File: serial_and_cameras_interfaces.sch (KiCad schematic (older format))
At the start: 60 parts, among them J13 533980471, J15 533980471, J16 533980471, J17 533980471, J2 WE_68715014522, U16 NTS0102GT, U17 NTS0104PW,118, U18 MAX485EESA, U5 NTS0102GT, U6 PCA9547BS

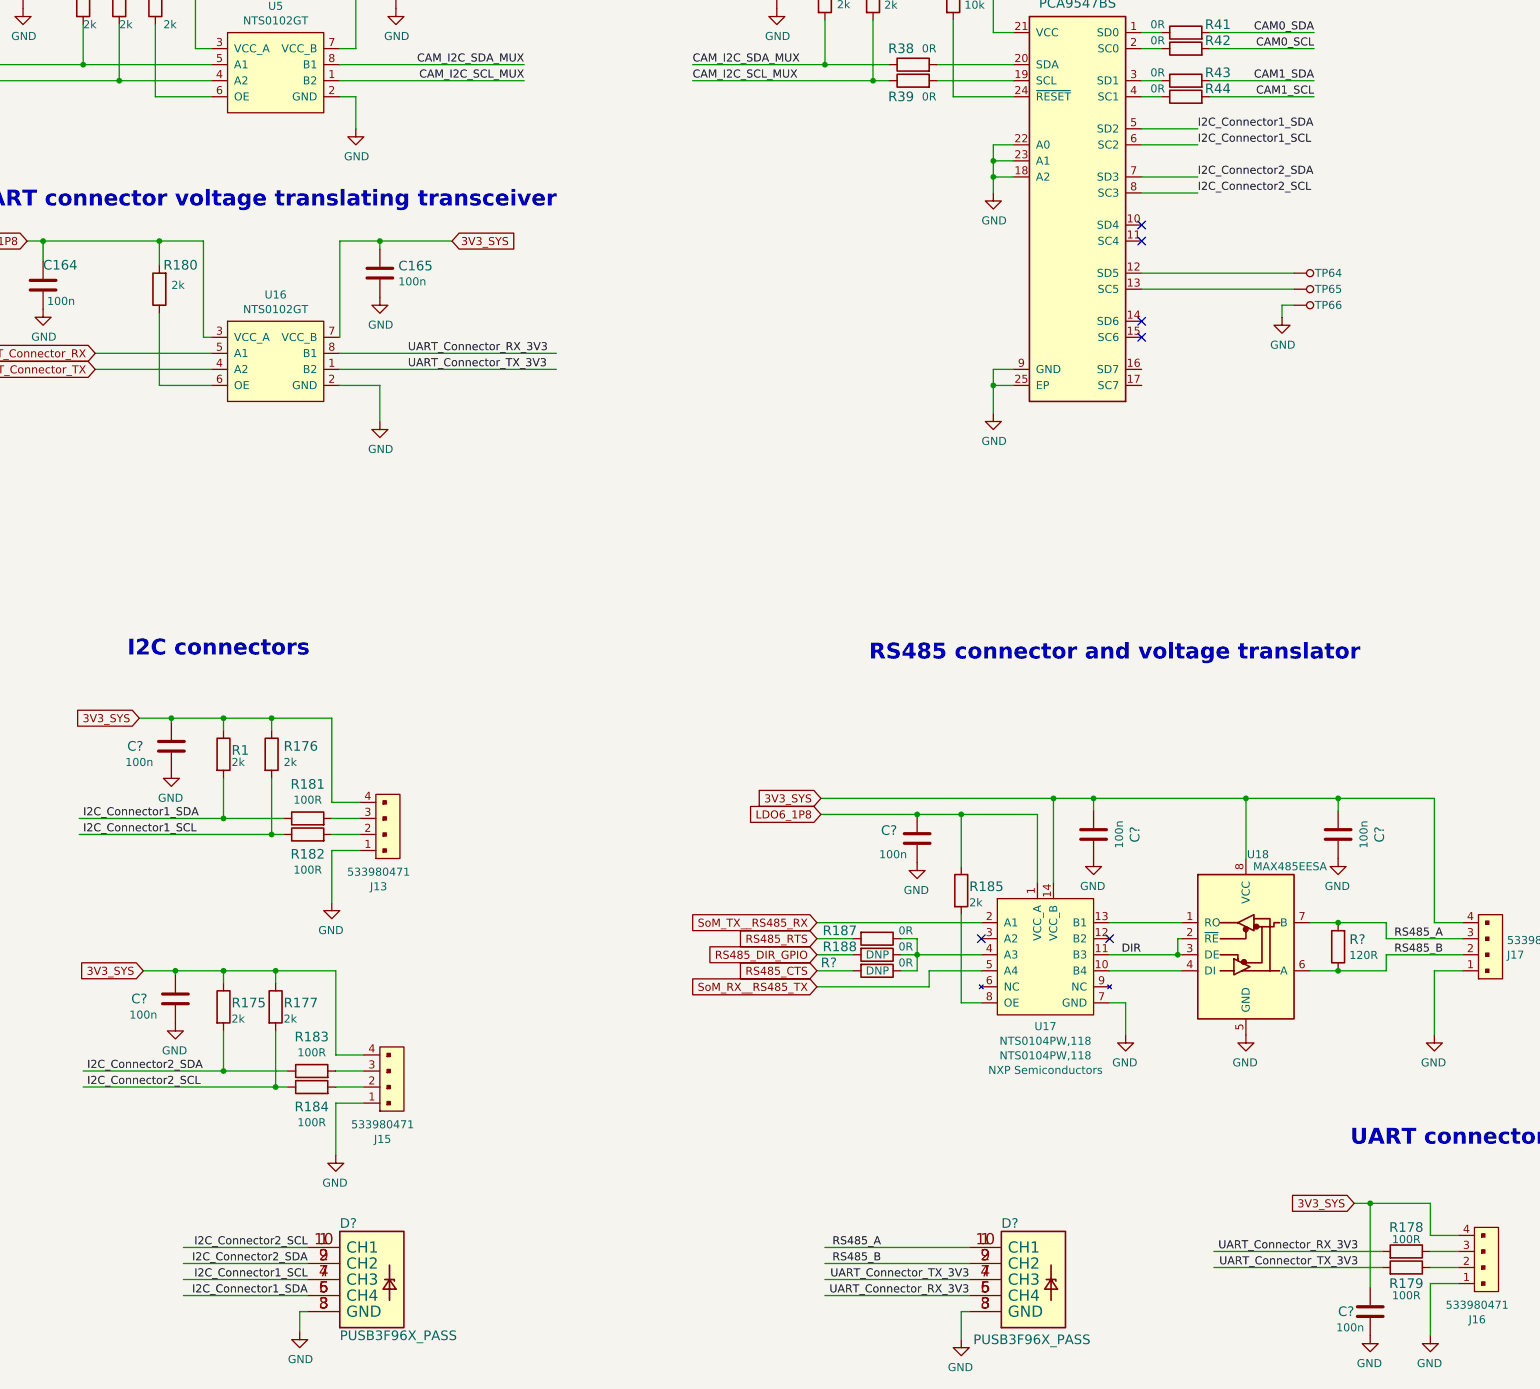
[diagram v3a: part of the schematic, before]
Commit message: Placement of serial interface connectors components
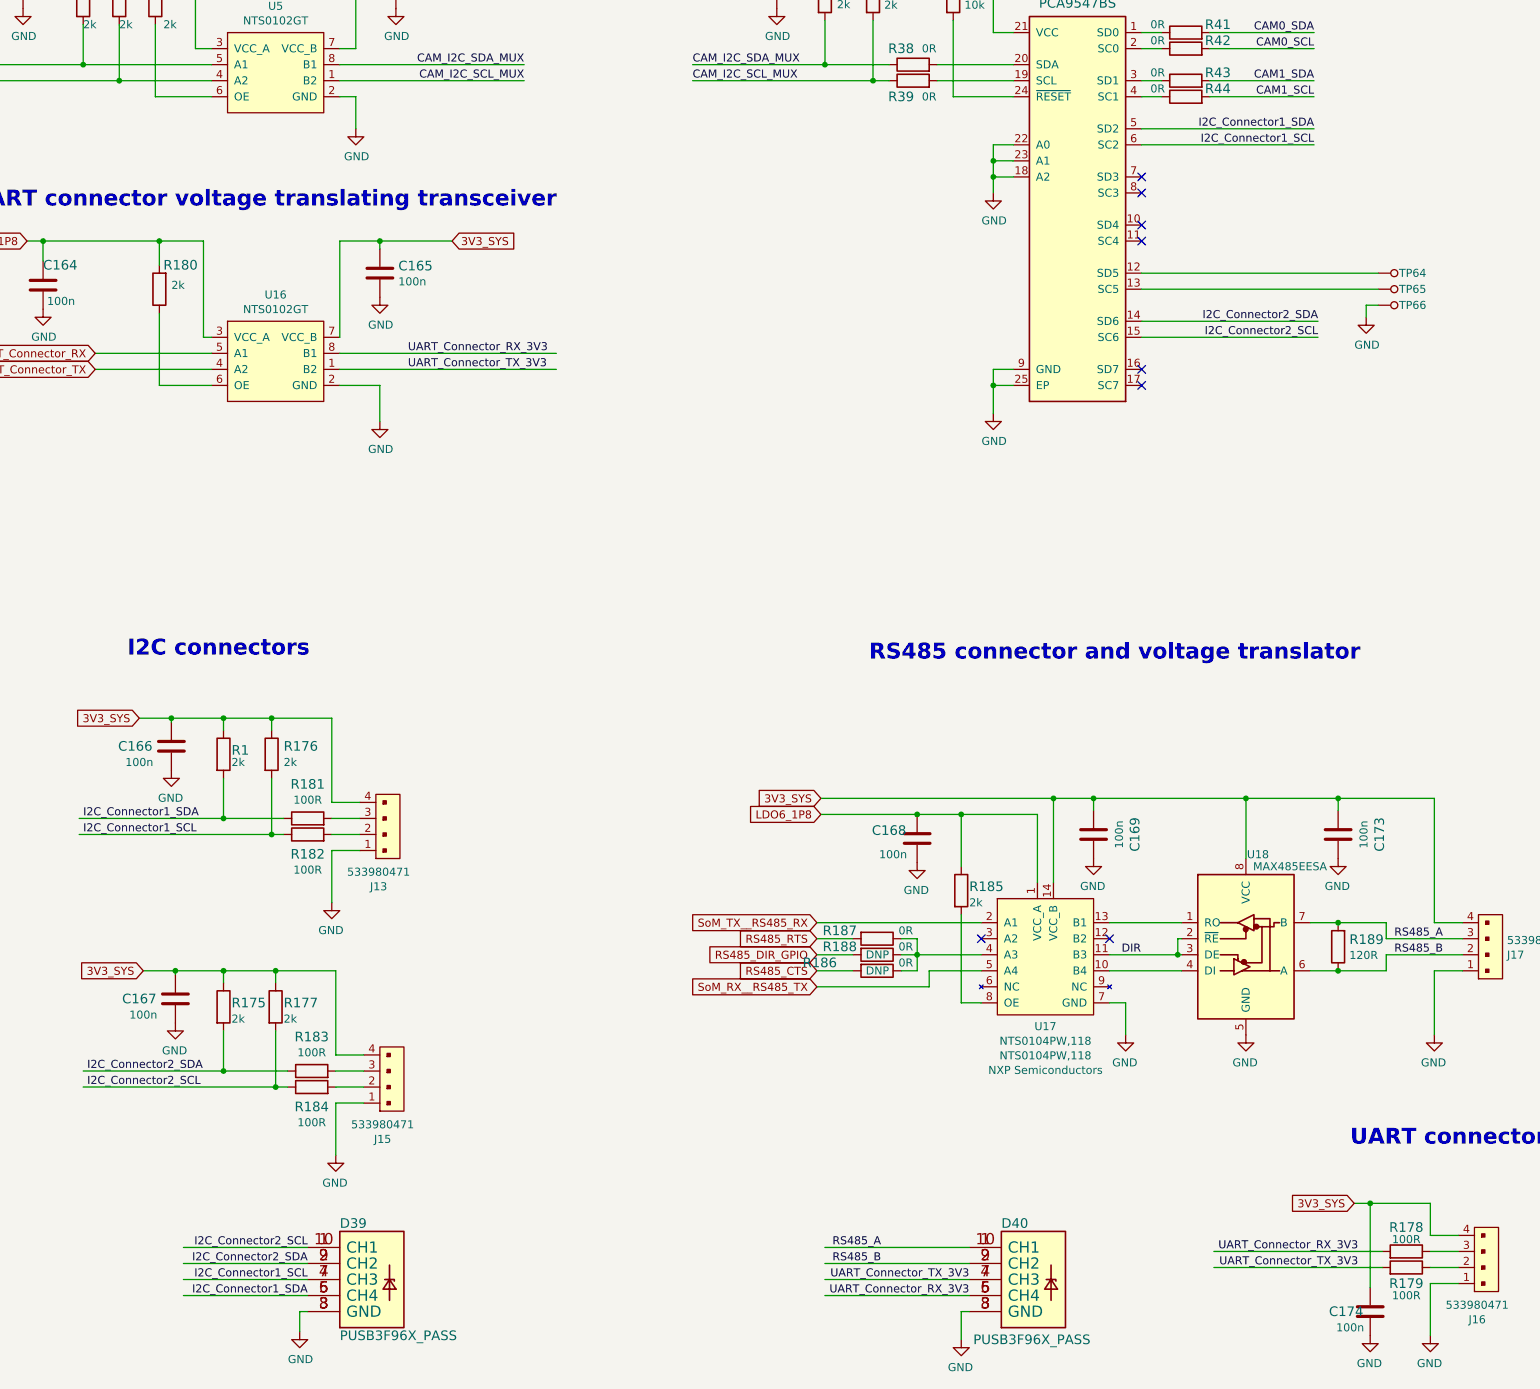
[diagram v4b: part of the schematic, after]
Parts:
- gave numbers to parts that had none: 10
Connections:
- no-connect marks 20 -> 22
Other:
- moved on the sheet: TP64, TP65, TP66
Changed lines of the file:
@@
 NoConn ~ 8750 3325
 NoConn ~ 8750 3425
-NoConn ~ 8750 3925
-NoConn ~ 8750 4025
 $Comp
 L sc606-baseboard:R_0R_0402 R41
@@
 Camera connector\n
 Wire Wire Line
-	8750 2725 9100 2725
-Wire Wire Line
-	8750 2825 9100 2825
+	8750 2725 9825 2725
+Wire Wire Line
+	8750 2825 9825 2825
 $Comp
 L sc606-baseboard:TP_SMD_0_75MM TP?
 U 1 1 640131A9
-P 9800 3625
+P 10325 3625
 AR Path="/61D43102/640131A9" Ref="TP?"  Part="1"
 AR Path="/61D49F95/640131A9" Ref="TP64"  Part="1"
-F 0 "TP64" V 9800 3425 50  0000 L CNN
-F 1 "TP_SMD_1_5MM" H 9800 3525 50  0001 C CNN
-F 2 "sc606-baseboard-footprints:TP-R-1.5" H 10000 3825 60  0001 L CNN
-F 3 "" H 10000 3925 60  0001 L CNN
-	1    9800 3625
+F 0 "TP64" V 10325 3425 50  0000 L CNN
+F 1 "TP_SMD_1_5MM" H 10325 3525 50  0001 C CNN
+F 2 "sc606-baseboard-footprints:TP-R-1.5" H 10525 3825 60  0001 L CNN
+F 3 "" H 10525 3925 60  0001 L CNN
+	1    10325 3625
 	0    -1   -1   0
 $EndComp
@@
 L sc606-baseboard:TP_SMD_0_75MM TP?
 U 1 1 640131AF
-P 9800 3725
+P 10325 3725
 AR Path="/61D43102/640131AF" Ref="TP?"  Part="1"
 AR Path="/61D49F95/640131AF" Ref="TP65"  Part="1"
-F 0 "TP65" V 9800 3525 50  0000 L CNN
-F 1 "TP_SMD_1_5MM" H 9800 3625 50  0001 C CNN
-F 2 "sc606-baseboard-footprints:TP-R-1.5" H 10000 3925 60  0001 L CNN
-F 3 "" H 10000 4025 60  0001 L CNN
-	1    9800 3725
+F 0 "TP65" V 10325 3525 50  0000 L CNN
+F 1 "TP_SMD_1_5MM" H 10325 3625 50  0001 C CNN
+F 2 "sc606-baseboard-footprints:TP-R-1.5" H 10525 3925 60  0001 L CNN
+F 3 "" H 10525 4025 60  0001 L CNN
+	1    10325 3725
 	0    -1   -1   0
 $EndComp
 Wire Wire Line
-	8750 3625 9700 3625
-Wire Wire Line
-	8750 3725 9700 3725
+	8750 3625 10225 3625
+Wire Wire Line
+	8750 3725 10225 3725
 $Comp
 L sc606-baseboard:TP_SMD_0_75MM TP?
 U 1 1 640131B7
-P 9800 3825
+P 10325 3825
 AR Path="/61D43102/640131B7" Ref="TP?"  Part="1"
 AR Path="/61D49F95/640131B7" Ref="TP66"  Part="1"
-F 0 "TP66" V 9800 3625 50  0000 L CNN
-F 1 "TP_SMD_1_5MM" H 9800 3725 50  0001 C CNN
-F 2 "sc606-baseboard-footprints:TP-R-1.5" H 10000 4025 60  0001 L CNN
-F 3 "" H 10000 4125 60  0001 L CNN
-	1    9800 3825
+F 0 "TP66" V 10325 3625 50  0000 L CNN
+F 1 "TP_SMD_1_5MM" H 10325 3725 50  0001 C CNN
+F 2 "sc606-baseboard-footprints:TP-R-1.5" H 10525 4025 60  0001 L CNN
+F 3 "" H 10525 4125 60  0001 L CNN
+	1    10325 3825
 	0    -1   -1   0
 $EndComp
 Wire Wire Line
-	9700 3825 9625 3825
-Wire Wire Line
-	9625 3825 9625 3900
+	10225 3825 10150 3825
+Wire Wire Line
+	10150 3825 10150 3900
 $Comp
 L sc606-baseboard:GND #PWR0228
 U 1 1 640131BF
-P 9625 3900
-F 0 "#PWR0228" H 9625 3650 50  0001 C CNN
-F 1 "GND" H 9630 3727 50  0000 C CNN
-F 2 "" H 9625 3900 50  0001 C CNN
-F 3 "" H 9625 3900 50  0001 C CNN
-	1    9625 3900
+P 10150 3900
+F 0 "#PWR0228" H 10150 3650 50  0001 C CNN
+F 1 "GND" H 10155 3727 50  0000 C CNN
+F 2 "" H 10150 3900 50  0001 C CNN
+F 3 "" H 10150 3900 50  0001 C CNN
+	1    10150 3900
 	1    0    0    -1
 $EndComp
@@
 	13525 6450 14600 6450
 Wire Wire Line
-	8750 3025 9100 3025
-Wire Wire Line
-	8750 3125 9100 3125
+	8750 3925 9850 3925
+Wire Wire Line
+	8750 4025 9850 4025
 Text Notes 2425 6025 0    99   ~ 20
 I2C connectors\n
@@
 	0    1    1    0
 $EndComp
-Text Label 9100 2725 0    50   ~ 0
+Text Label 9825 2725 2    50   ~ 0
 I2C_Connector1_SDA
-Text Label 9100 2825 0    50   ~ 0
+Text Label 9825 2825 2    50   ~ 0
 I2C_Connector1_SCL
-Text Label 9100 3025 0    50   ~ 0
+Text Label 9850 3925 2    50   ~ 0
 I2C_Connector2_SDA
-Text Label 9100 3125 0    50   ~ 0
+Text Label 9850 4025 2    50   ~ 0
 I2C_Connector2_SCL
 Text Label 2150 7025 0    50   ~ 0
@@
 $EndComp
 $Comp
-L sc606-baseboard:C_100n_0402 C?
+L sc606-baseboard:C_100n_0402 C173
 U 1 1 6237CE5F
 P 9975 7125
-F 0 "C?" V 10233 7125 60  0000 C CNN
+F 0 "C173" V 10233 7125 60  0000 C CNN
 F 1 "C_100n_0402" H 9975 6975 60  0001 C CNN
 F 2 "sc606-baseboard-footprints:0402-cap" H 10175 7325 60  0001 L CNN
@@
 $EndComp
 $Comp
-L sc606-baseboard:GND #PWR?
+L sc606-baseboard:GND #PWR0244
 U 1 1 6238011F
 P 9975 7275
-F 0 "#PWR?" H 9975 7025 50  0001 C CNN
+F 0 "#PWR0244" H 9975 7025 50  0001 C CNN
 F 1 "GND" H 9980 7102 50  0000 C CNN
 F 2 "" H 9975 7275 50  0001 C CNN
@@
 $EndComp
 $Comp
-L antmicroResistors0603:R_120R_0603 R?
+L antmicroResistors0603:R_120R_0603 R189
 U 1 1 62401FF8
 P 9975 7825
-F 0 "R?" V 10020 7755 60  0000 R CNN
+F 0 "R189" V 10020 7755 60  0000 R CNN
 F 1 "R_120R_0603" H 9975 7675 60  0001 C CNN
 F 2 "antmicro-footprints:0603-res" H 10175 8025 60  0001 L CNN
@@
 AR Path="/61F60810/6244A886" Ref="D?"  Part="1"
 AR Path="/63348E64/6244A886" Ref="D?"  Part="1"
-AR Path="/61D49F95/6244A886" Ref="D?"  Part="1"
-F 0 "D?" H 7875 10250 60  0000 L CNN
+AR Path="/61D49F95/6244A886" Ref="D40"  Part="1"
+F 0 "D40" H 7875 10250 60  0000 L CNN
 F 1 "PUSB3F96X_PASS" H 7700 9525 60  0000 L CNN
 F 2 "sc606-baseboard-footprints:PUSB3F96X" H 8075 9350 60  0001 C CNN
@@
 AR Path="/61F60810/6248C6BD" Ref="D?"  Part="1"
 AR Path="/63348E64/6248C6BD" Ref="D?"  Part="1"
-AR Path="/61D49F95/6248C6BD" Ref="D?"  Part="1"
-F 0 "D?" H 3750 10250 60  0000 L CNN
+AR Path="/61D49F95/6248C6BD" Ref="D39"  Part="1"
+F 0 "D39" H 3750 10250 60  0000 L CNN
 F 1 "PUSB3F96X_PASS" H 3750 9550 60  0000 L CNN
 F 2 "sc606-baseboard-footprints:PUSB3F96X" H 3950 9350 60  0001 C CNN
@@
 I2C_Connector1_SCL
 $Comp
-L sc606-baseboard:GND #PWR?
+L sc606-baseboard:GND #PWR0237
 U 1 1 624FA1E5
 P 3500 10225
-F 0 "#PWR?" H 3500 9975 50  0001 C CNN
+F 0 "#PWR0237" H 3500 9975 50  0001 C CNN
 F 1 "GND" H 3505 10052 50  0000 C CNN
 F 2 "" H 3500 10225 50  0001 C CNN
@@
 $EndComp
 $Comp
-L sc606-baseboard:GND #PWR?
+L sc606-baseboard:GND #PWR0241
 U 1 1 624FDF10
 P 7625 10275
-F 0 "#PWR?" H 7625 10025 50  0001 C CNN
+F 0 "#PWR0241" H 7625 10025 50  0001 C CNN
 F 1 "GND" H 7630 10102 50  0000 C CNN
 F 2 "" H 7625 10275 50  0001 C CNN
@@
 $EndComp
 $Comp
-L sc606-baseboard:C_100n_0402 C?
+L sc606-baseboard:C_100n_0402 C169
 U 1 1 622D6B57
 P 8450 7125
-F 0 "C?" V 8708 7125 60  0000 C CNN
+F 0 "C169" V 8708 7125 60  0000 C CNN
 F 1 "C_100n_0402" H 8450 6975 60  0001 C CNN
 F 2 "sc606-baseboard-footprints:0402-cap" H 8650 7325 60  0001 L CNN
@@
 $EndComp
 $Comp
-L sc606-baseboard:GND #PWR?
+L sc606-baseboard:GND #PWR0242
 U 1 1 622D6B5D
 P 8450 7275
-F 0 "#PWR?" H 8450 7025 50  0001 C CNN
+F 0 "#PWR0242" H 8450 7025 50  0001 C CNN
 F 1 "GND" H 8455 7102 50  0000 C CNN
 F 2 "" H 8450 7275 50  0001 C CNN
@@
 DIR
 $Comp
-L antmicroResistors0402:R_0R_0402 R?
+L antmicroResistors0402:R_0R_0402 R186
 U 1 1 6233B85C
 P 7100 7975
-F 0 "R?" H 7350 7925 60  0000 L CNN
+F 0 "R186" H 7350 7925 60  0000 L CNN
 F 1 "R_0R_0402" H 7100 7825 60  0001 C CNN
 F 2 "antmicro-footprints:0402-res" H 7300 8175 60  0001 L CNN
@@
 	7425 7975 7750 7975
 $Comp
-L sc606-baseboard:C_100n_0402 C?
+L sc606-baseboard:C_100n_0402 C168
 U 1 1 624F1A6A
 P 7350 7150
-F 0 "C?" H 7175 7200 60  0000 C CNN
+F 0 "C168" H 7175 7200 60  0000 C CNN
 F 1 "C_100n_0402" H 7350 7000 60  0001 C CNN
 F 2 "sc606-baseboard-footprints:0402-cap" H 7550 7350 60  0001 L CNN
@@
 $EndComp
 $Comp
-L sc606-baseboard:GND #PWR?
+L sc606-baseboard:GND #PWR0240
 U 1 1 624F1A70
 P 7350 7300
-F 0 "#PWR?" H 7350 7050 50  0001 C CNN
+F 0 "#PWR0240" H 7350 7050 50  0001 C CNN
 F 1 "GND" H 7355 7127 50  0000 C CNN
 F 2 "" H 7350 7300 50  0001 C CNN
@@
 	10575 8375 10575 7975
 $Comp
-L sc606-baseboard:C_100n_0402 C?
+L sc606-baseboard:C_100n_0402 C174
 U 1 1 626566A0
 P 10175 10100
-F 0 "C?" H 10025 10100 60  0000 C CNN
+F 0 "C174" H 10025 10100 60  0000 C CNN
 F 1 "C_100n_0402" H 10175 9950 60  0001 C CNN
 F 2 "sc606-baseboard-footprints:0402-cap" H 10375 10300 60  0001 L CNN
@@
 $EndComp
 $Comp
-L sc606-baseboard:GND #PWR?
+L sc606-baseboard:GND #PWR0245
 U 1 1 626566A6
 P 10175 10250
-F 0 "#PWR?" H 10175 10000 50  0001 C CNN
+F 0 "#PWR0245" H 10175 10000 50  0001 C CNN
 F 1 "GND" H 10180 10077 50  0000 C CNN
 F 2 "" H 10175 10250 50  0001 C CNN
@@
 	7625 10100 7675 10100
 $Comp
-L sc606-baseboard:C_100n_0402 C?
+L sc606-baseboard:C_100n_0402 C166
 U 1 1 6280DA5A
 P 2700 6575
-F 0 "C?" H 2475 6575 60  0000 C CNN
+F 0 "C166" H 2475 6575 60  0000 C CNN
 F 1 "C_100n_0402" H 2700 6425 60  0001 C CNN
 F 2 "sc606-baseboard-footprints:0402-cap" H 2900 6775 60  0001 L CNN
@@
 $EndComp
 $Comp
-L sc606-baseboard:GND #PWR?
+L sc606-baseboard:GND #PWR0172
 U 1 1 6280DA60
 P 2700 6725
-F 0 "#PWR?" H 2700 6475 50  0001 C CNN
+F 0 "#PWR0172" H 2700 6475 50  0001 C CNN
 F 1 "GND" H 2705 6552 50  0000 C CNN
 F 2 "" H 2700 6725 50  0001 C CNN
@@
 	3875 7125 3700 7125
 $Comp
-L sc606-baseboard:GND #PWR?
+L sc606-baseboard:GND #PWR0238
 U 1 1 6280DA87
 P 3700 7550
-F 0 "#PWR?" H 3700 7300 50  0001 C CNN
+F 0 "#PWR0238" H 3700 7300 50  0001 C CNN
 F 1 "GND" H 3705 7377 50  0000 C CNN
 F 2 "" H 3700 7550 50  0001 C CNN
@@
 	3350 8050 3350 7975
 $Comp
-L sc606-baseboard:C_100n_0402 C?
+L sc606-baseboard:C_100n_0402 C167
 U 1 1 629F5179
 P 2725 8150
-F 0 "C?" H 2500 8150 60  0000 C CNN
+F 0 "C167" H 2500 8150 60  0000 C CNN
 F 1 "C_100n_0402" H 2725 8000 60  0001 C CNN
 F 2 "sc606-baseboard-footprints:0402-cap" H 2925 8350 60  0001 L CNN
@@
 $EndComp
 $Comp
-L sc606-baseboard:GND #PWR?
+L sc606-baseboard:GND #PWR0179
 U 1 1 629F517F
 P 2725 8300
-F 0 "#PWR?" H 2725 8050 50  0001 C CNN
+F 0 "#PWR0179" H 2725 8050 50  0001 C CNN
 F 1 "GND" H 2730 8127 50  0000 C CNN
 F 2 "" H 2725 8300 50  0001 C CNN
@@
 	3900 8700 3725 8700
 $Comp
-L sc606-baseboard:GND #PWR?
+L sc606-baseboard:GND #PWR0239
 U 1 1 629F518A
 P 3725 9125
-F 0 "#PWR?" H 3725 8875 50  0001 C CNN
+F 0 "#PWR0239" H 3725 8875 50  0001 C CNN
 F 1 "GND" H 3730 8952 50  0000 C CNN
 F 2 "" H 3725 9125 50  0001 C CNN
@@
 Text GLabel 2225 4125 0    50   Input ~ 0
 UART_Connector_RX
+NoConn ~ 8750 3025
+NoConn ~ 8750 3125
+NoConn ~ 8750 4225
+NoConn ~ 8750 4325
 $EndSCHEMATC

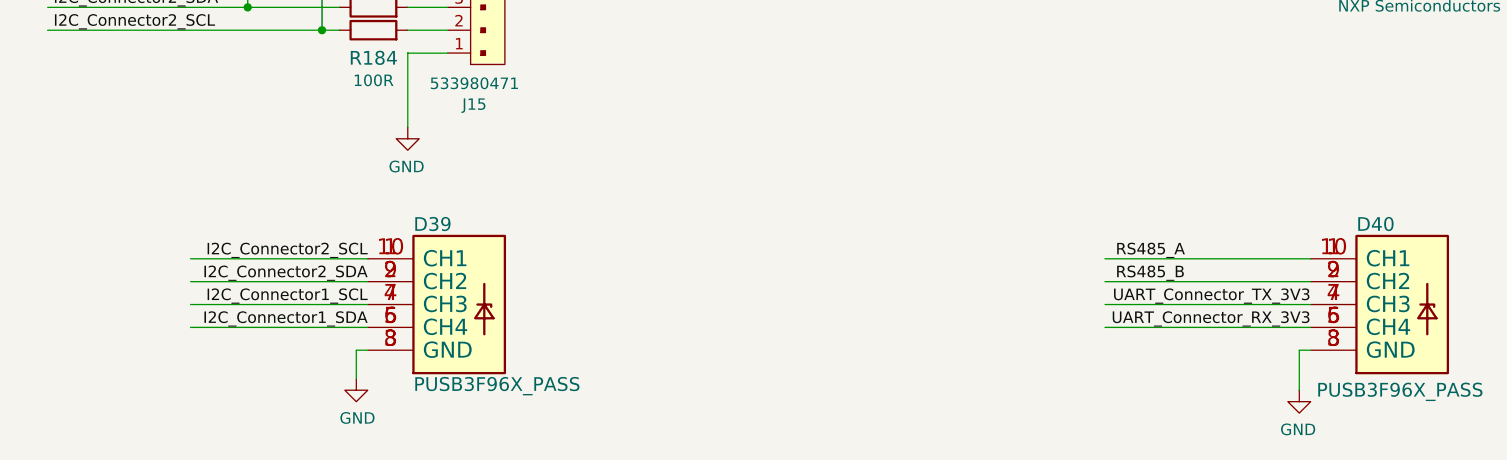
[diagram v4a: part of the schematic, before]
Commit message: Finished routing serial interface connectors
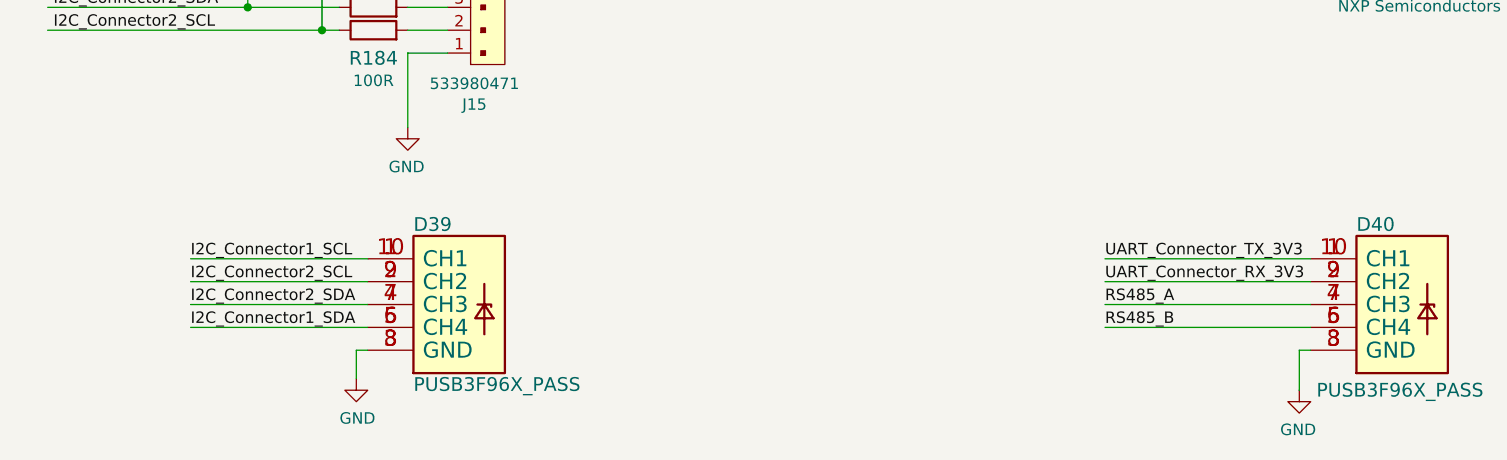
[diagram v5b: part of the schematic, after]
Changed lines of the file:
@@
 Wire Wire Line
 	9975 7975 10275 7975
-Text Label 7125 9700 2    50   ~ 0
+Text Label 6775 9900 0    50   ~ 0
 RS485_A
-Text Label 7125 9800 2    50   ~ 0
+Text Label 6775 10000 0    50   ~ 0
 RS485_B
-Text Label 7675 10000 2    50   ~ 0
+Text Label 6775 9800 0    50   ~ 0
 UART_Connector_RX_3V3
-Text Label 7675 9900 2    50   ~ 0
+Text Label 6775 9700 0    50   ~ 0
 UART_Connector_TX_3V3
 $Comp
@@
 	1    0    0    -1
 $EndComp
-Text Label 3550 9800 2    50   ~ 0
+Text Label 2775 9900 0    50   ~ 0
 I2C_Connector2_SDA
-Text Label 3550 9700 2    50   ~ 0
+Text Label 2775 9800 0    50   ~ 0
 I2C_Connector2_SCL
-Text Label 3550 10000 2    50   ~ 0
+Text Label 2775 10000 0    50   ~ 0
 I2C_Connector1_SDA
-Text Label 3550 9900 2    50   ~ 0
+Text Label 2775 9700 0    50   ~ 0
 I2C_Connector1_SCL
 $Comp
